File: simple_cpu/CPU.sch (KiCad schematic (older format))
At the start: 6 parts

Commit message: Update CPU.
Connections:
- net ~SCLK~ is gone; now on net SCLK: U?.6 (SCK), U?.6 (SCK)
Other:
- moved on the sheet: R?, U?

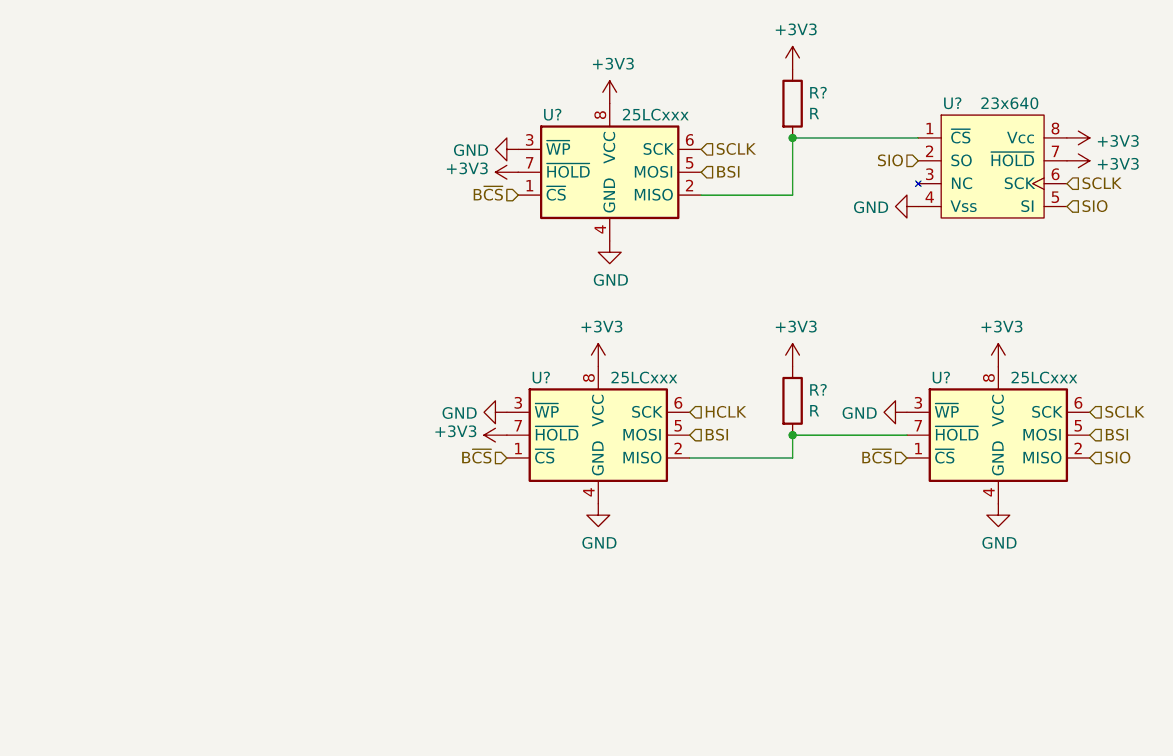
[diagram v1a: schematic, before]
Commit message: Update CPU schematic.
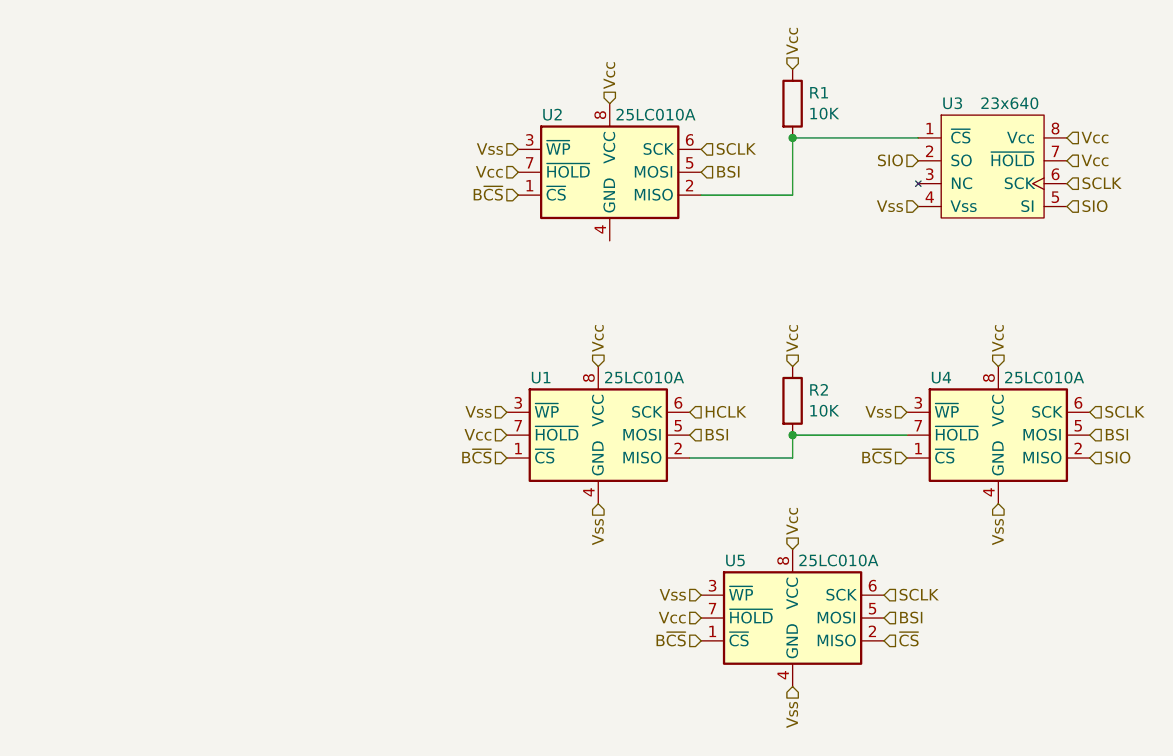
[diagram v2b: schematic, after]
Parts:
- added U5: 25LC010A, symbol Memory_EEPROM:25LCxxx
- R1, R2: renamed from R?; value R -> 10K
- U1, U2, U4: renamed from U?; value 25LCxxx -> 25LC010A
- gave numbers to parts that had none: 1
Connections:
- net BSI: now also U5.5 (MOSI)
- net B~CS~: now also U5.1 (~CS)
- net SCLK: now also U5.6 (SCK)
- net +3V3 renamed Vcc
- net Vcc: now also U5.7 (~HOLD), U5.8 (VCC)
- net GND renamed Vss
- net Vss: now also U5.3 (~WP), U5.4 (GND); no longer U2.4 (GND)
- new net ~CS~: U5.2 (MISO)
